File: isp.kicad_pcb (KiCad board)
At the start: 2 copper layers, 52.6 x 31.8 mm, 5 parts, among them J1 AVR-ISP-6, SW1 SW_Push, U2 PRO_MICRO

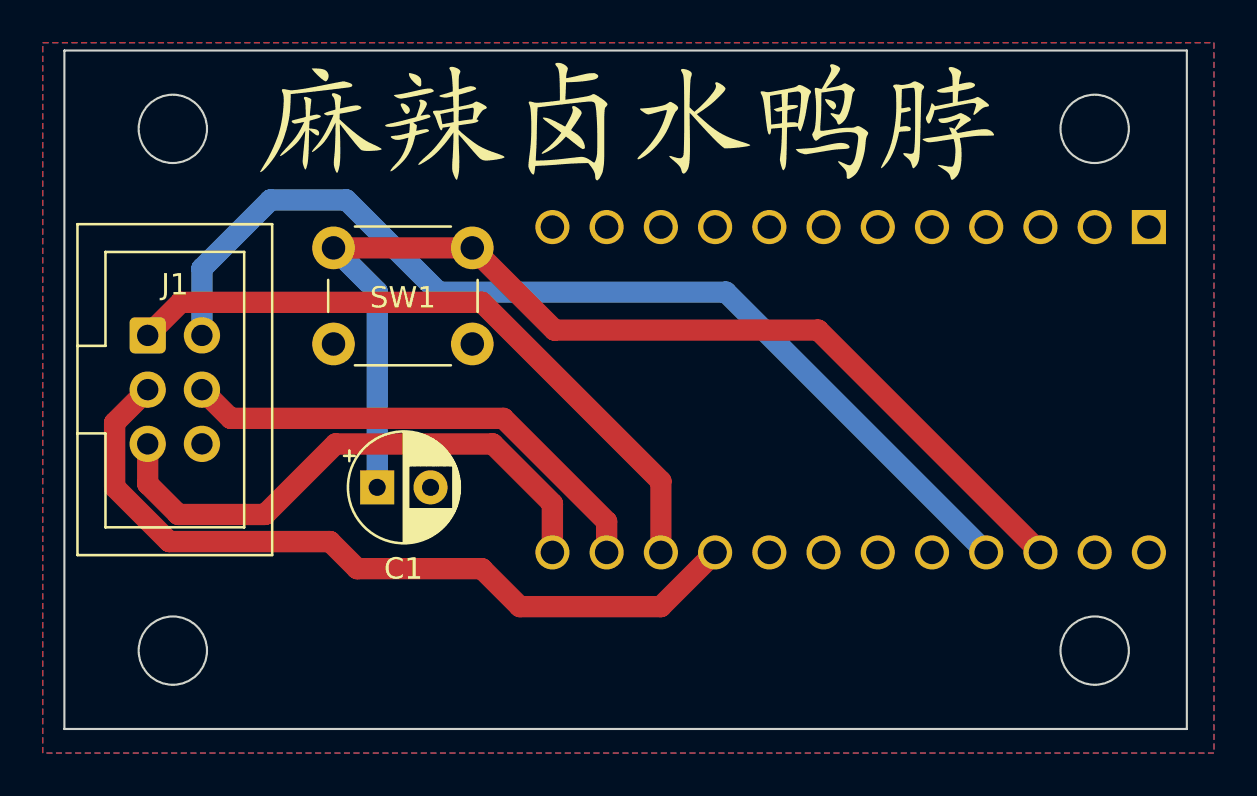
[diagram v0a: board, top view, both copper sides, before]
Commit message: add breakout header
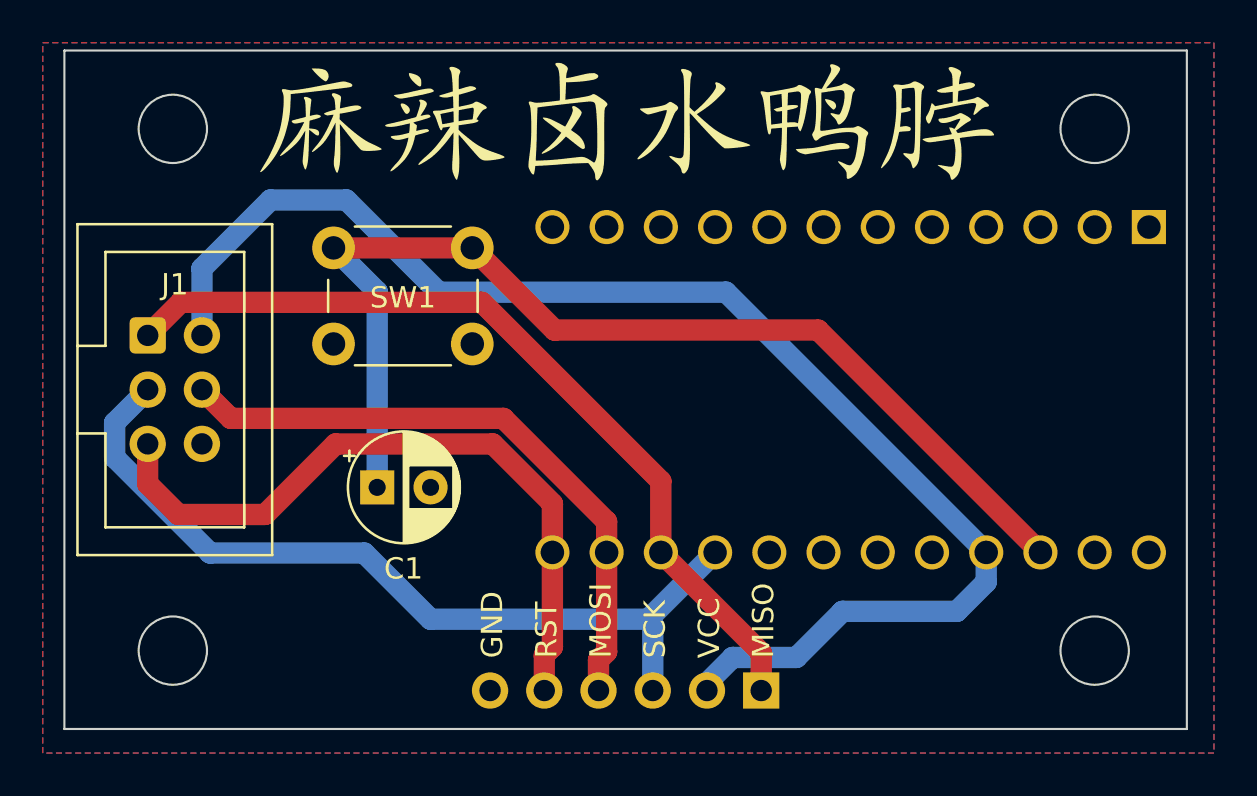
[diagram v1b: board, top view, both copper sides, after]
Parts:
- added J2: Conn_01x06, Connector_PinHeader_2.54mm:PinHeader_1x06_P2.54mm_Vertical, F.Cu at (170.6, 105.5)
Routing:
- net Net-(J1-VCC): track 48.0 -> 64.8 mm
- net Net-(J1-MISO): track 31.5 -> 39.9 mm
- net Net-(J1-MOSI): track 23.0 -> 29.6 mm
- net Net-(J1-~{RST}): track 26.2 -> 32.9 mm
- net Net-(J1-SCK): track 36.7 -> 39.8 mm
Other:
- board text added: "GND"
- board text added: "MISO"
- board text added: "MOSI"
- board text added: "RST"
- board text added: "SCK"
- board text added: "VCC"
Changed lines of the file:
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@@
     )
   )
+  (footprint "Connector_PinHeader_2.54mm:PinHeader_1x06_P2.54mm_Vertical" (layer "F.Cu")
+    (at 170.561 105.53 -90)
+    (descr "Through hole straight pin header, 1x06, 2.54mm pitch, single row")
+    (tags "Through hole pin header THT 1x06 2.54mm single row")
+    (property "Sheetfile" "isp.kicad_sch")
+    (property "Sheetname" "")
+    (property "ki_description" "Generic connector, single row, 01x06, script generated (kicad-library-utils/schlib/autogen/connector/)")
+    (property "ki_keywords" "connector")
+    (attr through_hole)
+    (fp_text reference "J2" (at 0 -2.33 90) (layer "F.SilkS") hide
+        (effects (font (size 1 1) (thickness 0.15)))
+    )
+    (fp_text value "Conn_01x06" (at 0 15.03 90) (layer "F.Fab") hide
+        (effects (font (size 1 1) (thickness 0.15)))
+    )
+    (fp_text user "${REFERENCE}" (at 0 6.35) (layer "F.Fab")
+        (effects (font (size 1 1) (thickness 0.15)))
+    )
+    (fp_line (start -1.8 -1.8) (end -1.8 14.5)
+      (stroke (width 0.05) (type solid)) (layer "F.CrtYd"))
+    (fp_line (start -1.8 14.5) (end 1.8 14.5)
+      (stroke (width 0.05) (type solid)) (layer "F.CrtYd"))
+    (fp_line (start 1.8 -1.8) (end -1.8 -1.8)
+      (stroke (width 0.05) (type solid)) (layer "F.CrtYd"))
+    (fp_line (start 1.8 14.5) (end 1.8 -1.8)
+      (stroke (width 0.05) (type solid)) (layer "F.CrtYd"))
+    (fp_line (start -1.27 -0.635) (end -0.635 -1.27)
+      (stroke (width 0.1) (type solid)) (layer "F.Fab"))
+    (fp_line (start -1.27 13.97) (end -1.27 -0.635)
+      (stroke (width 0.1) (type solid)) (layer "F.Fab"))
+    (fp_line (start -0.635 -1.27) (end 1.27 -1.27)
+      (stroke (width 0.1) (type solid)) (layer "F.Fab"))
+    (fp_line (start 1.27 -1.27) (end 1.27 13.97)
+      (stroke (width 0.1) (type solid)) (layer "F.Fab"))
+    (fp_line (start 1.27 13.97) (end -1.27 13.97)
+      (stroke (width 0.1) (type solid)) (layer "F.Fab"))
+    (pad "1" thru_hole rect (at 0 0 270) (size 1.7 1.7) (drill 1) (layers "*.Cu" "*.Mask")
+      (net 3 "Net-(J1-MISO)") (pinfunction "Pin_1") (pintype "passive"))
+    (pad "2" thru_hole oval (at 0 2.54 270) (size 1.7 1.7) (drill 1) (layers "*.Cu" "*.Mask")
+      (net 4 "Net-(J1-VCC)") (pinfunction "Pin_2") (pintype "passive"))
+    (pad "3" thru_hole oval (at 0 5.08 270) (size 1.7 1.7) (drill 1) (layers "*.Cu" "*.Mask")
+      (net 5 "Net-(J1-SCK)") (pinfunction "Pin_3") (pintype "passive"))
+    (pad "4" thru_hole oval (at 0 7.62 270) (size 1.7 1.7) (drill 1) (layers "*.Cu" "*.Mask")
+      (net 6 "Net-(J1-MOSI)") (pinfunction "Pin_4") (pintype "passive"))
+    (pad "5" thru_hole oval (at 0 10.16 270) (size 1.7 1.7) (drill 1) (layers "*.Cu" "*.Mask")
+      (net 7 "Net-(J1-~{RST})") (pinfunction "Pin_5") (pintype "passive"))
+    (pad "6" thru_hole oval (at 0 12.7 270) (size 1.7 1.7) (drill 1) (layers "*.Cu" "*.Mask")
+      (net 2 "GND") (pinfunction "Pin_6") (pintype "passive"))
+    (model "${KICAD6_3DMODEL_DIR}/Connector_PinHeader_2.54mm.3dshapes/PinHeader_1x06_P2.54mm_Vertical.wrl"
+      (offset (xyz 0 0 0))
+      (scale (xyz 1 1 1))
+      (rotate (xyz 0 0 0))
+    )
+  )
   (footprint "Capacitor_THT:CP_Radial_D5.0mm_P2.50mm" (layer "F.Cu")
     (at 152.573388 96.012)
@@
   (gr_circle (center 186.182 79.22) (end 188.682 79.22)
     (stroke (width 0.1) (type default)) (fill none) (layer "F.Fab"))
+  (gr_text "SCK" (at 166.1685 104.02 90) (layer "F.SilkS")
+    (effects (font (size 1 1) (thickness 0.15)) (justify left bottom))
+  )
+  (gr_text "MOSI" (at 163.6285 104.02 90) (layer "F.SilkS")
+    (effects (font (size 1 1) (thickness 0.15)) (justify left bottom))
+  )
+  (gr_text "RST" (at 161.0885 104.02 90) (layer "F.SilkS")
+    (effects (font (size 1 1) (thickness 0.15)) (justify left bottom))
+  )
+  (gr_text "VCC" (at 168.7085 104.02 90) (layer "F.SilkS")
+    (effects (font (size 1 1) (thickness 0.15)) (justify left bottom))
+  )
+  (gr_text "MISO" (at 171.2485 104.02 90) (layer "F.SilkS")
+    (effects (font (size 1 1) (thickness 0.15)) (justify left bottom))
+  )
+  (gr_text "GND" (at 158.5485 104.02 90) (layer "F.SilkS")
+    (effects (font (size 1 1) (thickness 0.15)) (justify left bottom))
+  )
   (segment (start 173.228 88.646) (end 160.8795 88.646) (width 1) (layer "F.Cu") (net 1))
   (segment (start 160.8795 88.646) (end 157.0285 84.795) (width 1) (layer "F.Cu") (net 1))
@@
   (segment (start 152.573388 86.839888) (end 152.573388 96.012) (width 1) (layer "B.Cu") (net 1))
   (segment (start 165.862 95.724336) (end 165.862 99.06) (width 1) (layer "F.Cu") (net 3))
+  (segment (start 170.561 105.53) (end 170.561 103.759) (width 1) (layer "F.Cu") (net 3))
   (segment (start 141.825 88.895) (end 143.375 87.345) (width 1) (layer "F.Cu") (net 3))
   (segment (start 157.482664 87.345) (end 165.862 95.724336) (width 1) (layer "F.Cu") (net 3))
   (segment (start 143.375 87.345) (end 157.482664 87.345) (width 1) (layer "F.Cu") (net 3))
+  (segment (start 170.561 103.759) (end 165.862 99.06) (width 1) (layer "F.Cu") (net 3))
+  (segment (start 174.37 101.82) (end 172.21 103.98) (width 1) (layer "B.Cu") (net 4))
+  (segment (start 179.73 101.82) (end 174.37 101.82) (width 1) (layer "B.Cu") (net 4))
   (segment (start 181.102 99.06) (end 168.91 86.868) (width 1) (layer "B.Cu") (net 4))
   (segment (start 147.574 82.55) (end 144.365 85.759) (width 1) (layer "B.Cu") (net 4))
+  (segment (start 181.102 99.06) (end 181.102 100.448) (width 1) (layer "B.Cu") (net 4))
   (segment (start 155.448 86.868) (end 151.13 82.55) (width 1) (layer "B.Cu") (net 4))
   (segment (start 151.13 82.55) (end 147.574 82.55) (width 1) (layer "B.Cu") (net 4))
+  (segment (start 169.223032 103.98) (end 168.021 105.182032) (width 1) (layer "B.Cu") (net 4))
+  (segment (start 172.21 103.98) (end 169.223032 103.98) (width 1) (layer "B.Cu") (net 4))
+  (segment (start 181.102 100.448) (end 179.73 101.82) (width 1) (layer "B.Cu") (net 4))
   (segment (start 144.365 85.759) (end 144.365 88.895) (width 1) (layer "B.Cu") (net 4))
+  (segment (start 168.021 105.182032) (end 168.021 105.53) (width 1) (layer "B.Cu") (net 4))
   (segment (start 168.91 86.868) (end 155.448 86.868) (width 1) (layer "B.Cu") (net 4))
-  (segment (start 159.258 101.6) (end 165.862 101.6) (width 1) (layer "F.Cu") (net 5))
-  (segment (start 140.275 95.998056) (end 142.828944 98.552) (width 1) (layer "F.Cu") (net 5))
-  (segment (start 157.48 99.822) (end 159.258 101.6) (width 1) (layer "F.Cu") (net 5))
-  (segment (start 141.825 91.435) (end 140.275 92.985) (width 1) (layer "F.Cu") (net 5))
-  (segment (start 142.828944 98.552) (end 150.368 98.552) (width 1) (layer "F.Cu") (net 5))
-  (segment (start 140.275 92.985) (end 140.275 95.998056) (width 1) (layer "F.Cu") (net 5))
-  (segment (start 151.638 99.822) (end 157.48 99.822) (width 1) (layer "F.Cu") (net 5))
-  (segment (start 150.368 98.552) (end 151.638 99.822) (width 1) (layer "F.Cu") (net 5))
-  (segment (start 165.862 101.6) (end 168.402 99.06) (width 1) (layer "F.Cu") (net 5))
+  (segment (start 140.275 92.985) (end 140.275 94.617032) (width 1) (layer "B.Cu") (net 5))
+  (segment (start 165.481 102.399) (end 165.272 102.19) (width 1) (layer "B.Cu") (net 5))
+  (segment (start 151.97 99.09) (end 155.07 102.19) (width 1) (layer "B.Cu") (net 5))
+  (segment (start 140.275 94.617032) (end 144.747968 99.09) (width 1) (layer "B.Cu") (net 5))
+  (segment (start 165.272 102.19) (end 168.402 99.06) (width 1) (layer "B.Cu") (net 5))
+  (segment (start 144.747968 99.09) (end 151.97 99.09) (width 1) (layer "B.Cu") (net 5))
+  (segment (start 141.825 91.435) (end 140.275 92.985) (width 1) (layer "B.Cu") (net 5))
+  (segment (start 165.481 105.53) (end 165.481 102.399) (width 1) (layer "B.Cu") (net 5))
+  (segment (start 155.07 102.19) (end 165.272 102.19) (width 1) (layer "B.Cu") (net 5))
+  (segment (start 162.941 105.53) (end 162.941 104.099) (width 1) (layer "F.Cu") (net 6))
   (segment (start 163.322 97.616944) (end 158.485056 92.78) (width 1) (layer "F.Cu") (net 6))
+  (segment (start 163.322 103.718) (end 163.322 99.06) (width 1) (layer "F.Cu") (net 6))
   (segment (start 158.485056 92.78) (end 145.71 92.78) (width 1) (layer "F.Cu") (net 6))
+  (segment (start 162.941 104.099) (end 163.322 103.718) (width 1) (layer "F.Cu") (net 6))
   (segment (start 145.71 92.78) (end 144.365 91.435) (width 1) (layer "F.Cu") (net 6))
   (segment (start 163.322 99.06) (end 163.322 97.616944) (width 1) (layer "F.Cu") (net 6))
+  (segment (start 160.401 105.53) (end 160.401 103.869) (width 1) (layer "F.Cu") (net 7))
   (segment (start 160.782 96.774) (end 157.988 93.98) (width 1) (layer "F.Cu") (net 7))
   (segment (start 143.256 97.282) (end 141.825 95.851) (width 1) (layer "F.Cu") (net 7))
+  (segment (start 160.782 103.488) (end 160.782 99.06) (width 1) (layer "F.Cu") (net 7))
   (segment (start 141.825 95.851) (end 141.825 93.975) (width 1) (layer "F.Cu") (net 7))
+  (segment (start 160.401 103.869) (end 160.782 103.488) (width 1) (layer "F.Cu") (net 7))
   (segment (start 160.782 99.06) (end 160.782 96.774) (width 1) (layer "F.Cu") (net 7))
   (segment (start 150.622 93.98) (end 147.32 97.282) (width 1) (layer "F.Cu") (net 7))
